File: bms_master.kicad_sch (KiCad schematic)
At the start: 80 parts, among them J1 Conn_01x02, J2 Conn_01x02, J3 Conn_01x02, J4 Conn_01x04, J5 Conn_01x04, J6 Conn_01x06, Q1 FDV303N, Q2 FDV304P, Q3 FDV304P, SW1 SW_Push, U1 TPS7B88, U2 MCP1700x-330xxMB, U3 STM32F103C8Tx, U4 SN65HVD1050D, U5 M24C64-R, U6 MAX6126, U7 MAX11163, U8 741G3157, Y1 8M

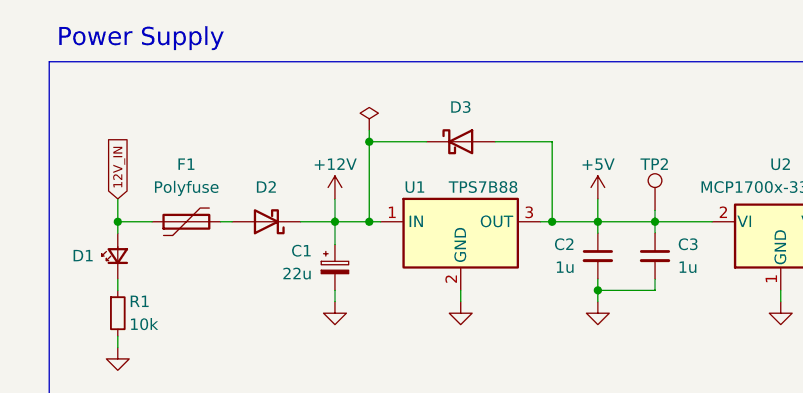
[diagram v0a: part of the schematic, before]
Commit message: *: Add 12V test point
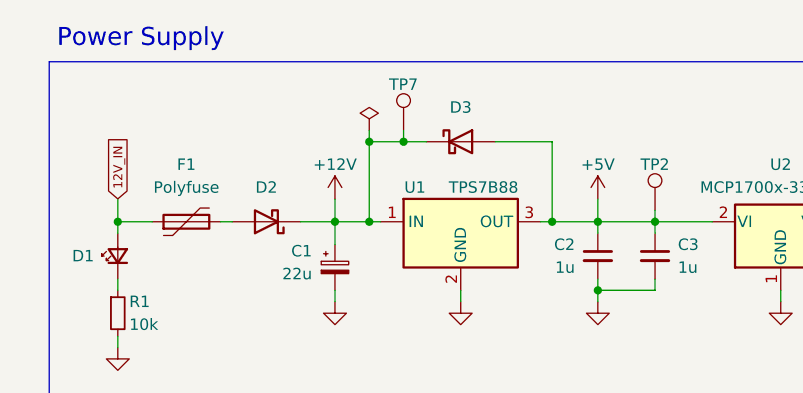
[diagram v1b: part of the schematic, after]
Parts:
- added TP7: TestPoint, TestPoint:TestPoint_Keystone_5000-5004_Miniature, symbol Connector:TestPoint
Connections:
- net +12V: now also TP7.1
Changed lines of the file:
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@@
 	)
 	(junction
+		(at 59.69 26.67)
+		(diameter 0)
+		(color 0 0 0 0)
+	)
+	(junction
 		(at 31.75 134.62)
 		(diameter 0)
@@
 	(wire
 		(pts
+			(xy 59.69 25.4) (xy 59.69 26.67)
+		)
+		(stroke
+			(width 0)
+			(type default)
+		)
+	)
+	(wire
+		(pts
 			(xy 93.98 139.7) (xy 101.6 139.7)
 		)
@@
 	(wire
 		(pts
-			(xy 62.23 26.67) (xy 55.88 26.67)
+			(xy 62.23 26.67) (xy 59.69 26.67)
 		)
 		(stroke
@@
 	(wire
 		(pts
+			(xy 59.69 26.67) (xy 55.88 26.67)
+		)
+		(stroke
+			(width 0)
+			(type default)
+		)
+	)
+	(wire
+		(pts
 			(xy 251.46 152.4) (xy 254 152.4)
 		)
@@
 					(unit 1)
 				)
+			)
+		)
+	)
+	(symbol
+		(lib_id "Connector:TestPoint")
+		(at 59.69 25.4 0)
+		(unit 1)
+		(exclude_from_sim no)
+		(in_bom yes)
+		(on_board yes)
+		(dnp no)
+		(property "Reference" "TP7"
+			(at 59.69 20.32 0)
+			(effects
+				(font
+					(size 1.27 1.27)
+				)
+			)
+		)
+		(property "Value" "TestPoint"
+			(at 62.23 23.3679 0)
+			(effects
+				(font
+					(size 1.27 1.27)
+				)
+				(justify left)
+				(hide yes)
+			)
+		)
+		(property "Footprint" "TestPoint:TestPoint_Keystone_5000-5004_Miniature"
+			(at 64.77 25.4 0)
+			(effects
+				(font
+					(size 1.27 1.27)
+				)
+				(hide yes)
+			)
+		)
+		(property "Datasheet" "~"
+			(at 64.77 25.4 0)
+			(effects
+				(font
+					(size 1.27 1.27)
+				)
+				(hide yes)
+			)
+		)
+		(property "Description" "test point"
+			(at 59.69 25.4 0)
+			(effects
+				(font
+					(size 1.27 1.27)
+				)
+				(hide yes)
+			)
+		)
+		(pin "1"
+		)
+		(instances
+			(project "bms_master"
+				(path "/ff788b45-a486-492a-a3f3-4e15ca08a026"
+					(reference "TP7")
+					(unit 1)
+				)

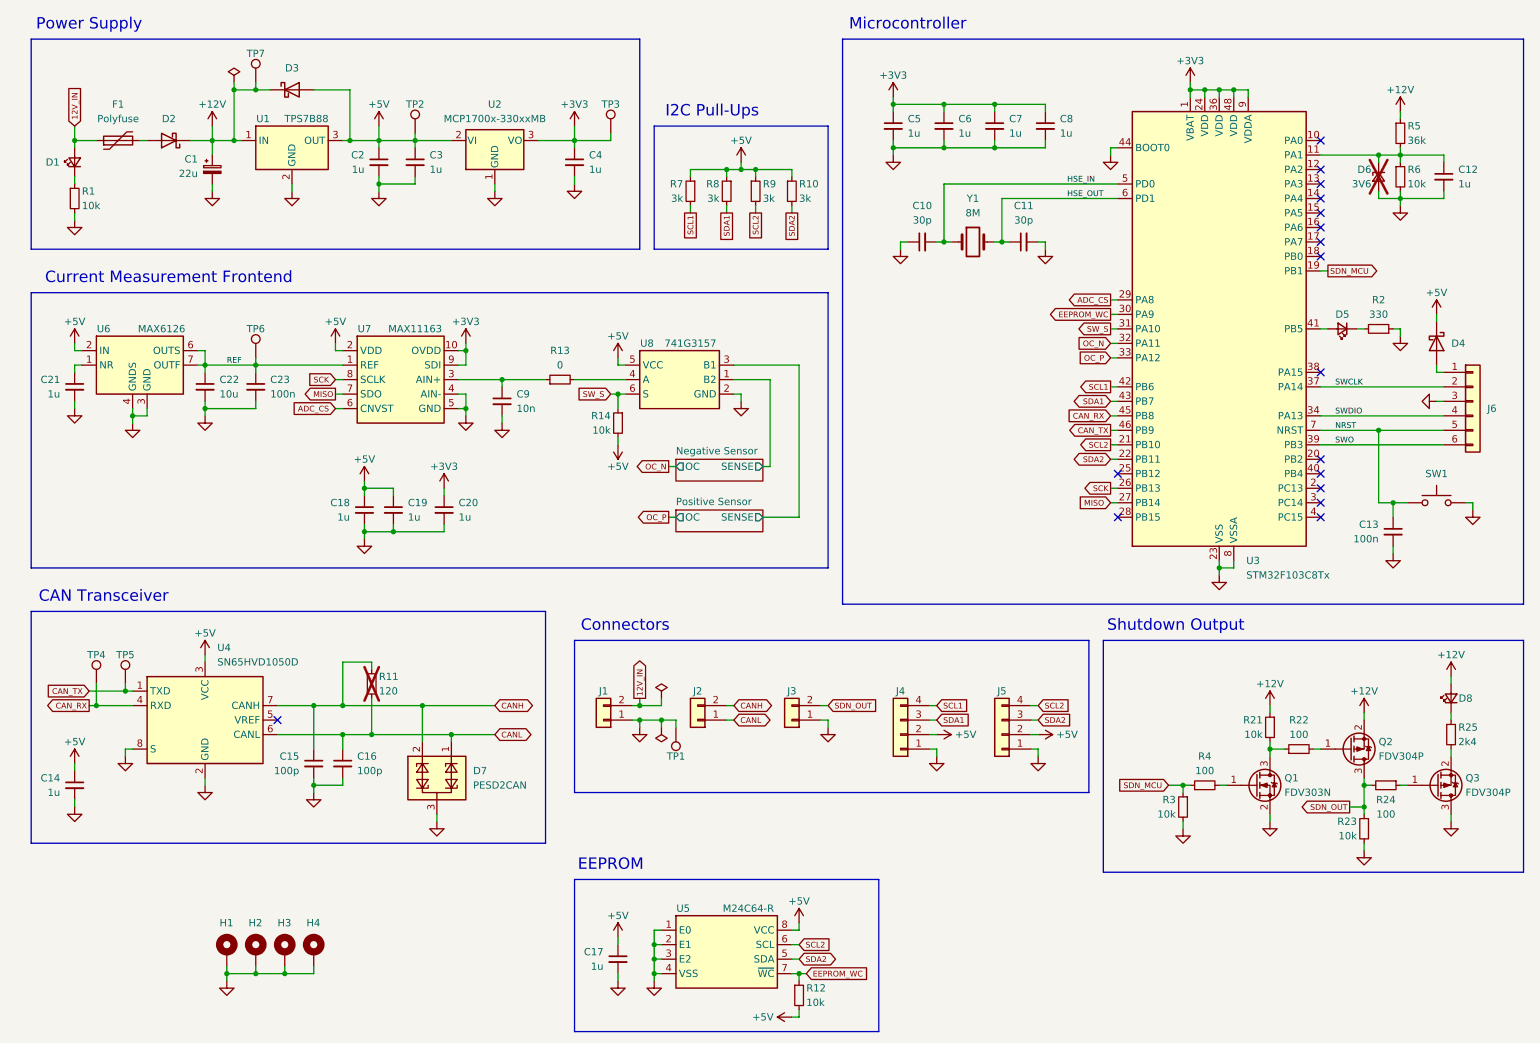
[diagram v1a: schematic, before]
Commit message: *: Use an eFuse on the 12 LVS input
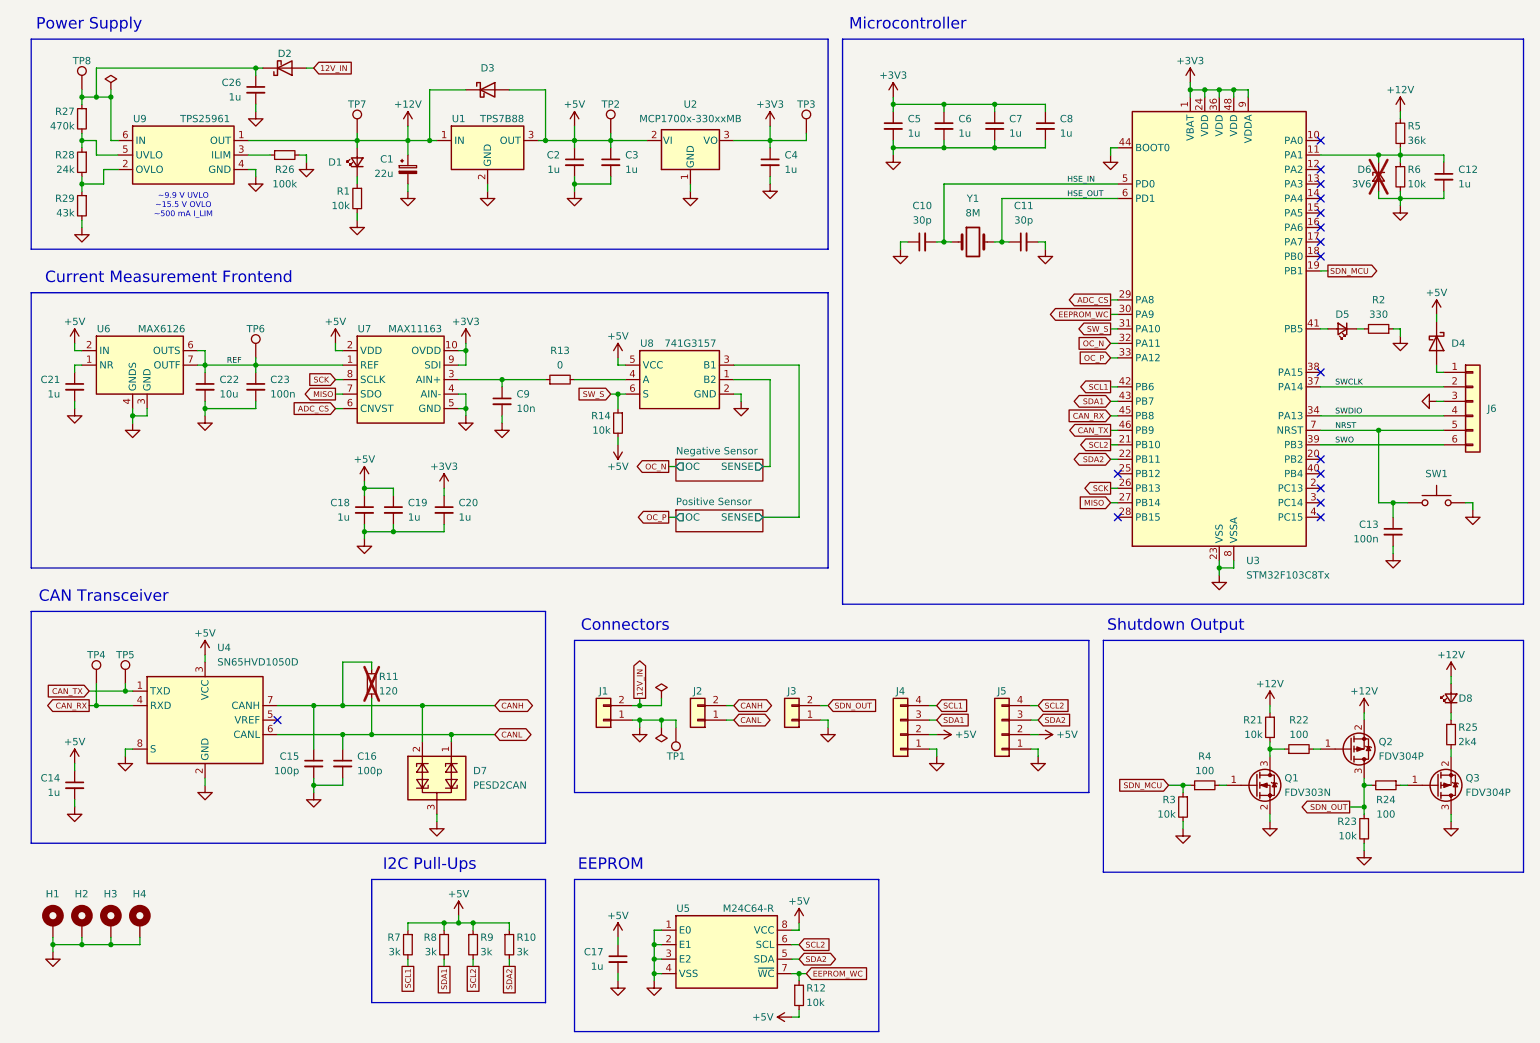
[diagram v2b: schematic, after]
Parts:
- removed F1: Polyfuse, Capacitor_SMD:C_0805_2012Metric, symbol Device:Polyfuse
- added C26: 1u, Capacitor_SMD:C_0603_1608Metric, symbol Device:C_Small
- added R26: 100k, Resistor_SMD:R_0603_1608Metric, symbol Device:R_Small
- added R27: 470k, Resistor_SMD:R_0603_1608Metric, symbol Device:R_Small
- added R28: 24k, Resistor_SMD:R_0603_1608Metric, symbol Device:R_Small
- added R29: 43k, Resistor_SMD:R_0603_1608Metric, symbol Device:R_Small
- added TP8: TestPoint, TestPoint:TestPoint_Keystone_5000-5004_Miniature, symbol Connector:TestPoint
- added U9: TPS25961, Package_SON:WSON-6-1EP_2x2mm_P0.65mm_EP1x1.6mm, symbol yfs:TPS25961
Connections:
- net +12V: now also D1.2 (A), U9.1 (OUT); no longer D2.1 (K)
- net 12V_IN: now also D2.2 (A); no longer D1.2 (A)
- net GND: now also C26.2, R26.2, R29.2, U9.4 (GND), U9.7 (GND)
- new net: C26.1, D2.1 (K), R27.1, TP8.1, U9.6 (IN)
- new net: R27.2, R28.1, U9.5 (UVLO)
- new net: R28.2, R29.1, U9.2 (OVLO)
- new net: R26.1, U9.3 (ILIM)
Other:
- note added: "~9.9 V UVLO ~15.5 V OVLO ~500 mA I_LIM"
- moved on the sheet: C1, C2, C3, C4, D1, D2, D3, H1, H2, H3, H4, R1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

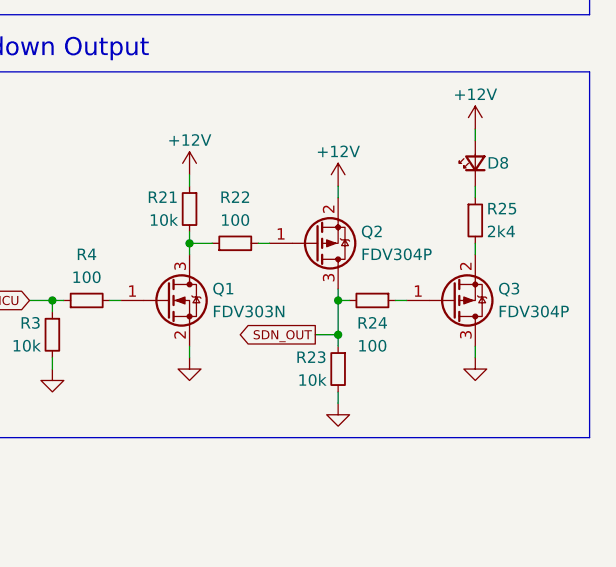
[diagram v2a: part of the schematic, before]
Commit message: *: Use more suitable MOSFETs in the shutdown circuit
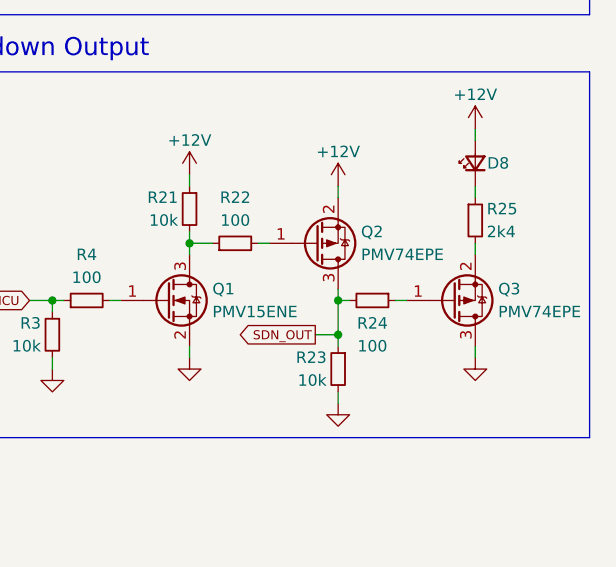
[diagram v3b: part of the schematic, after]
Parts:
- removed Q1: FDV303N, Package_TO_SOT_SMD:SOT-23, symbol yfs:FDV303N
- removed Q2, Q3: FDV304P, Package_TO_SOT_SMD:SOT-23, symbol yfs:FDV304P
- added Q1: PMV15ENE, Package_TO_SOT_SMD:SOT-23, symbol yfs:PMV15ENE
- added Q2, Q3: PMV74EPE, Package_TO_SOT_SMD:SOT-23, symbol yfs:PMV74EPE
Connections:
- net +12V: now also Q2.2 (S)
- net GND: now also Q1.2 (S), Q3.3 (D)
- net SDN_OUT: now also Q2.3 (D)
- net at R21.2, R22.1: now also Q1.3 (D)
- net at R25.2: now also Q3.2 (S)
- net at R4.2: now also Q1.1 (G)
- net at R24.1: now also Q3.1 (G)
- net at R22.2: now also Q2.1 (G)

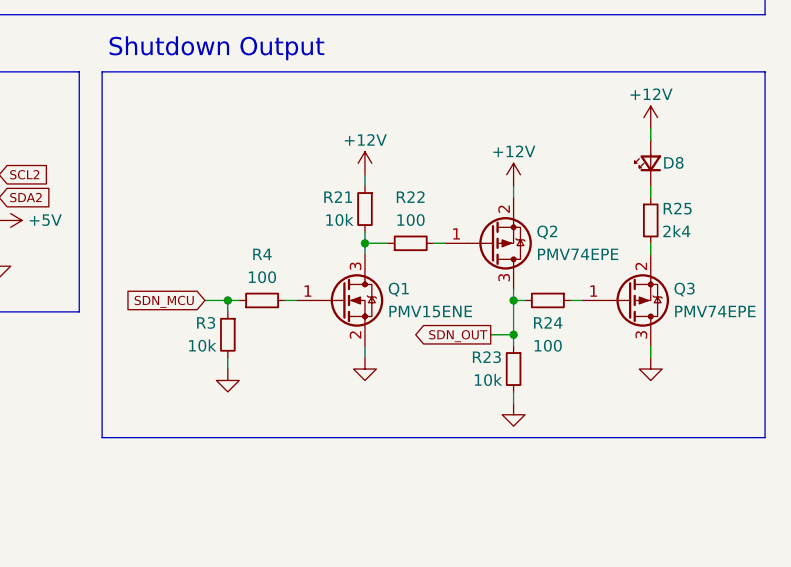
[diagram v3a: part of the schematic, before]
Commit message: *: Change shutdown MOSFET gate resistors to 1k
This provides more protection and reduces BOM count.
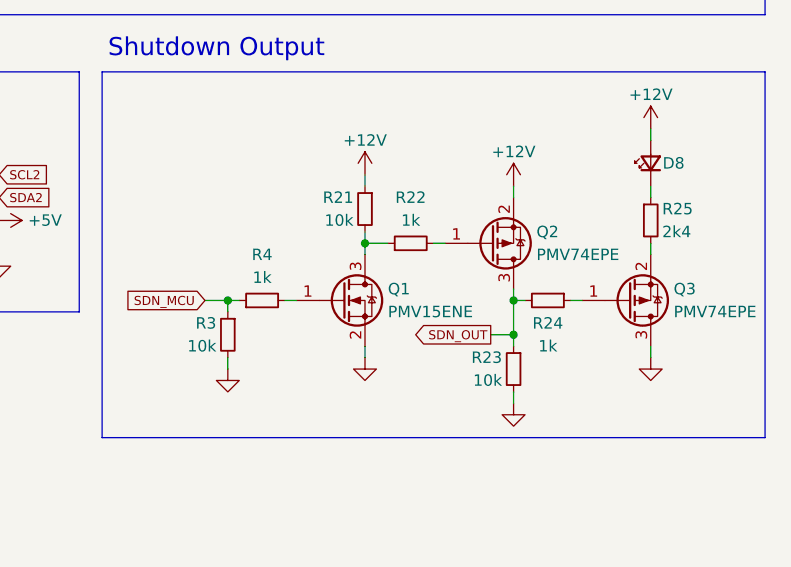
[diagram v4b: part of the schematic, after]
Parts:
- R22, R24, R4: value 100 -> 1k; Dist # C22775 -> C21190; Mfr # 0603WAF1000T5E -> 0603WAF1001T5E
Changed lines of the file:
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@@
 			)
 		)
-		(property "Value" "100"
+		(property "Value" "1k"
 			(at 257.81 153.67 90)
 			(effects
@@
 			)
 		)
-		(property "Dist #" "C22775"
+		(property "Dist #" "C21190"
 			(at 257.81 148.59 90)
 			(effects
@@
 			)
 		)
-		(property "Mfr #" "0603WAF1000T5E"
+		(property "Mfr #" "0603WAF1001T5E"
 			(at 257.81 148.59 90)
 			(effects
@@
 			)
 		)
-		(property "Value" "100"
+		(property "Value" "1k"
 			(at 226.06 146.05 90)
 			(effects
@@
 			)
 		)
-		(property "Dist #" "C22775"
+		(property "Dist #" "C21190"
 			(at 226.06 148.59 90)
 			(effects
@@
 			)
 		)
-		(property "Mfr #" "0603WAF1000T5E"
+		(property "Mfr #" "0603WAF1001T5E"
 			(at 226.06 148.59 90)
 			(effects
@@
 			)
 		)
-		(property "Value" "100"
+		(property "Value" "1k"
 			(at 242.57 139.7 90)
 			(effects
@@
 			)
 		)
-		(property "Dist #" "C22775"
+		(property "Dist #" "C21190"
 			(at 242.57 142.24 90)
 			(effects
@@
 			)
 		)
-		(property "Mfr #" "0603WAF1000T5E"
+		(property "Mfr #" "0603WAF1001T5E"
 			(at 242.57 142.24 90)
 			(effects

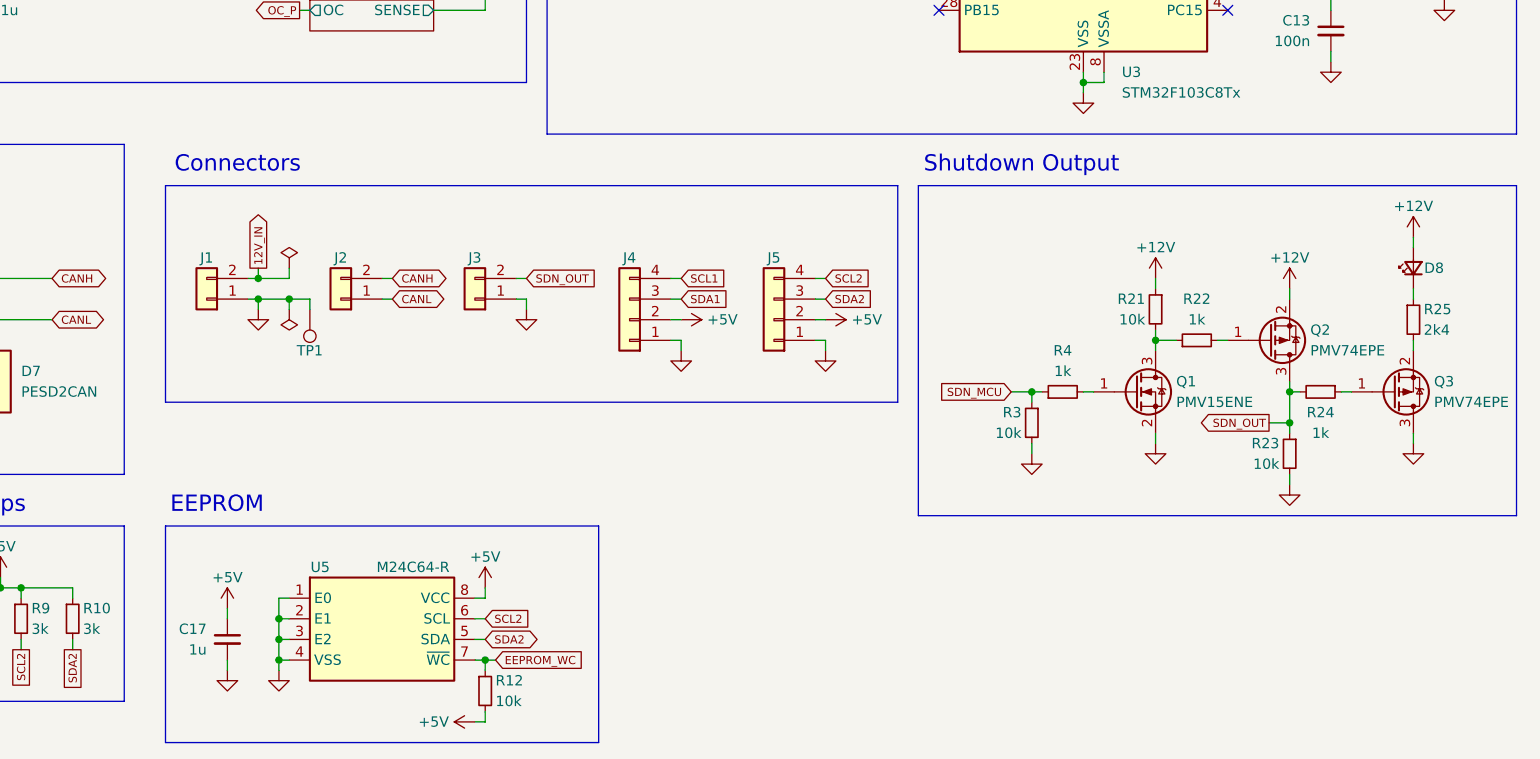
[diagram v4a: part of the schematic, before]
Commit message: *: Add a current limiting resistor to the shutdown output
This reduces the output level to around 10.9 volts.
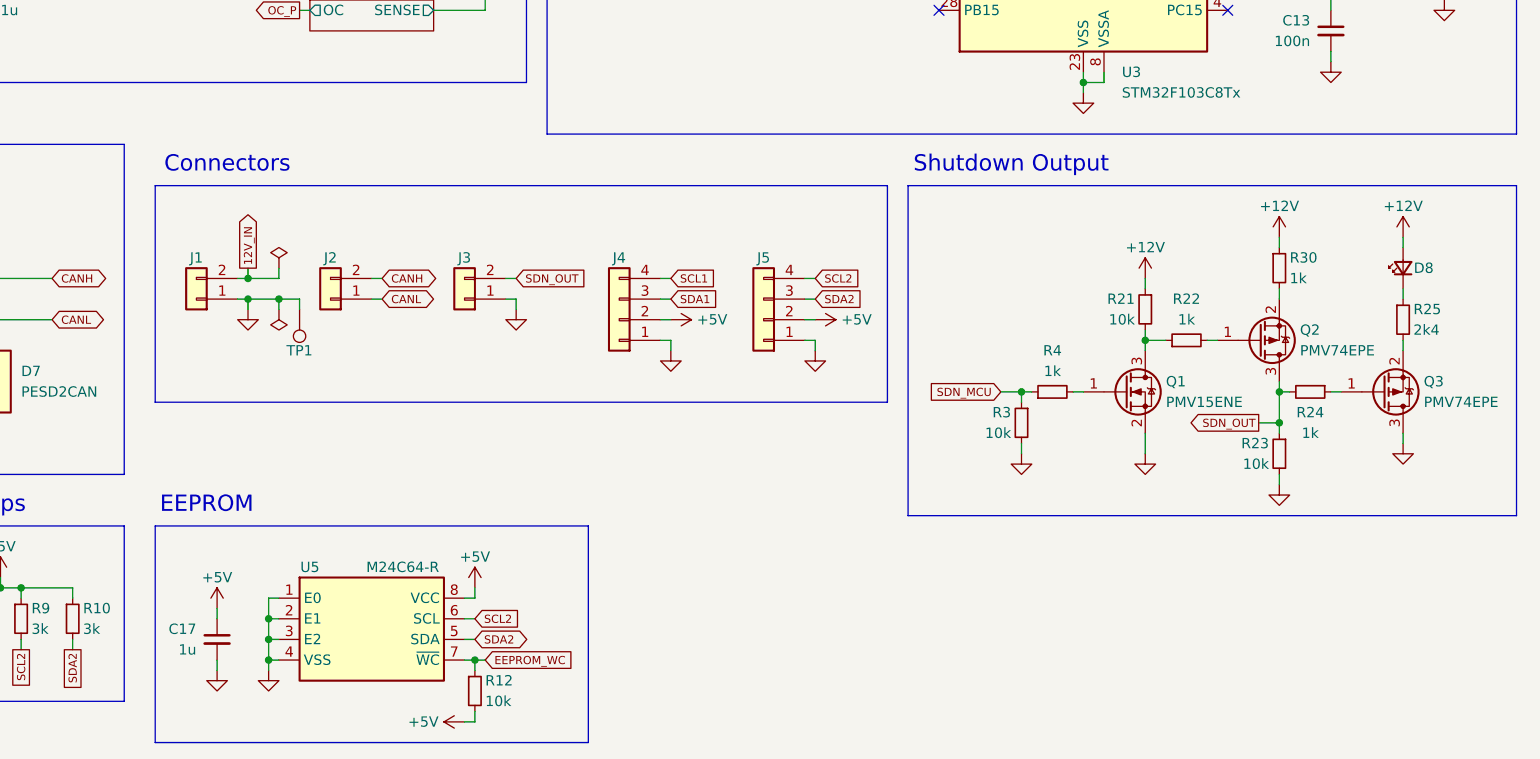
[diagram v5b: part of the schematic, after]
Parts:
- added R30: 1k, Resistor_SMD:R_0603_1608Metric, symbol Device:R_Small
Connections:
- net +12V: now also R30.1; no longer Q2.2 (S)
- new net: Q2.2 (S), R30.2
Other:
- moved on the sheet: C17, D8, J1, J2, J3, J4, J5, Q1, Q2, Q3, R12, R21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
